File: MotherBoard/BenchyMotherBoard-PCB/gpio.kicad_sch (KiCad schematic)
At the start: 29 parts, among them J8 FAN-CONN, Q1 SQ2310ES_SOT23, Q2 MMBT2222A, SW1 BOOT-SEL, U27 TMP100NA, U28 TMP100NA, U4 AM6254ATCGGAALW, Y1 24MHz

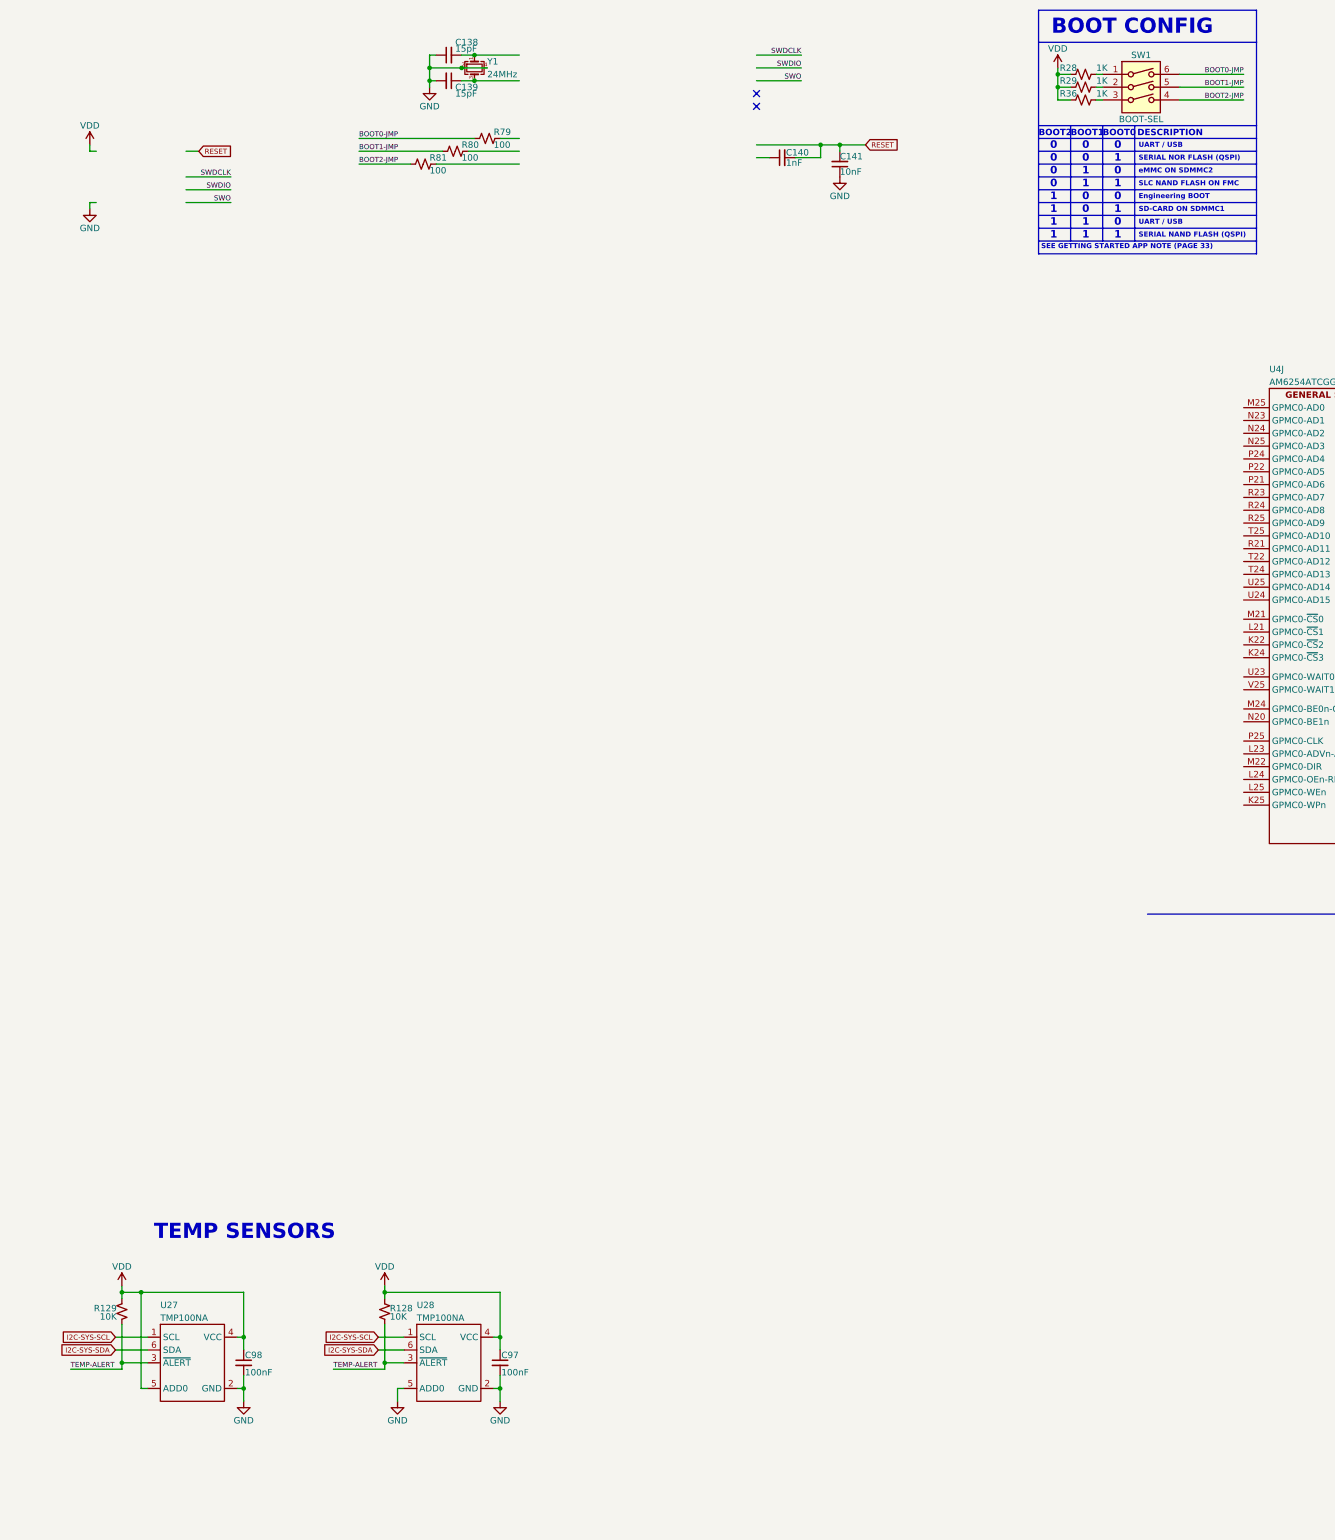
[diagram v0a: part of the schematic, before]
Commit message: Add new ethernet chip - KSZ9031
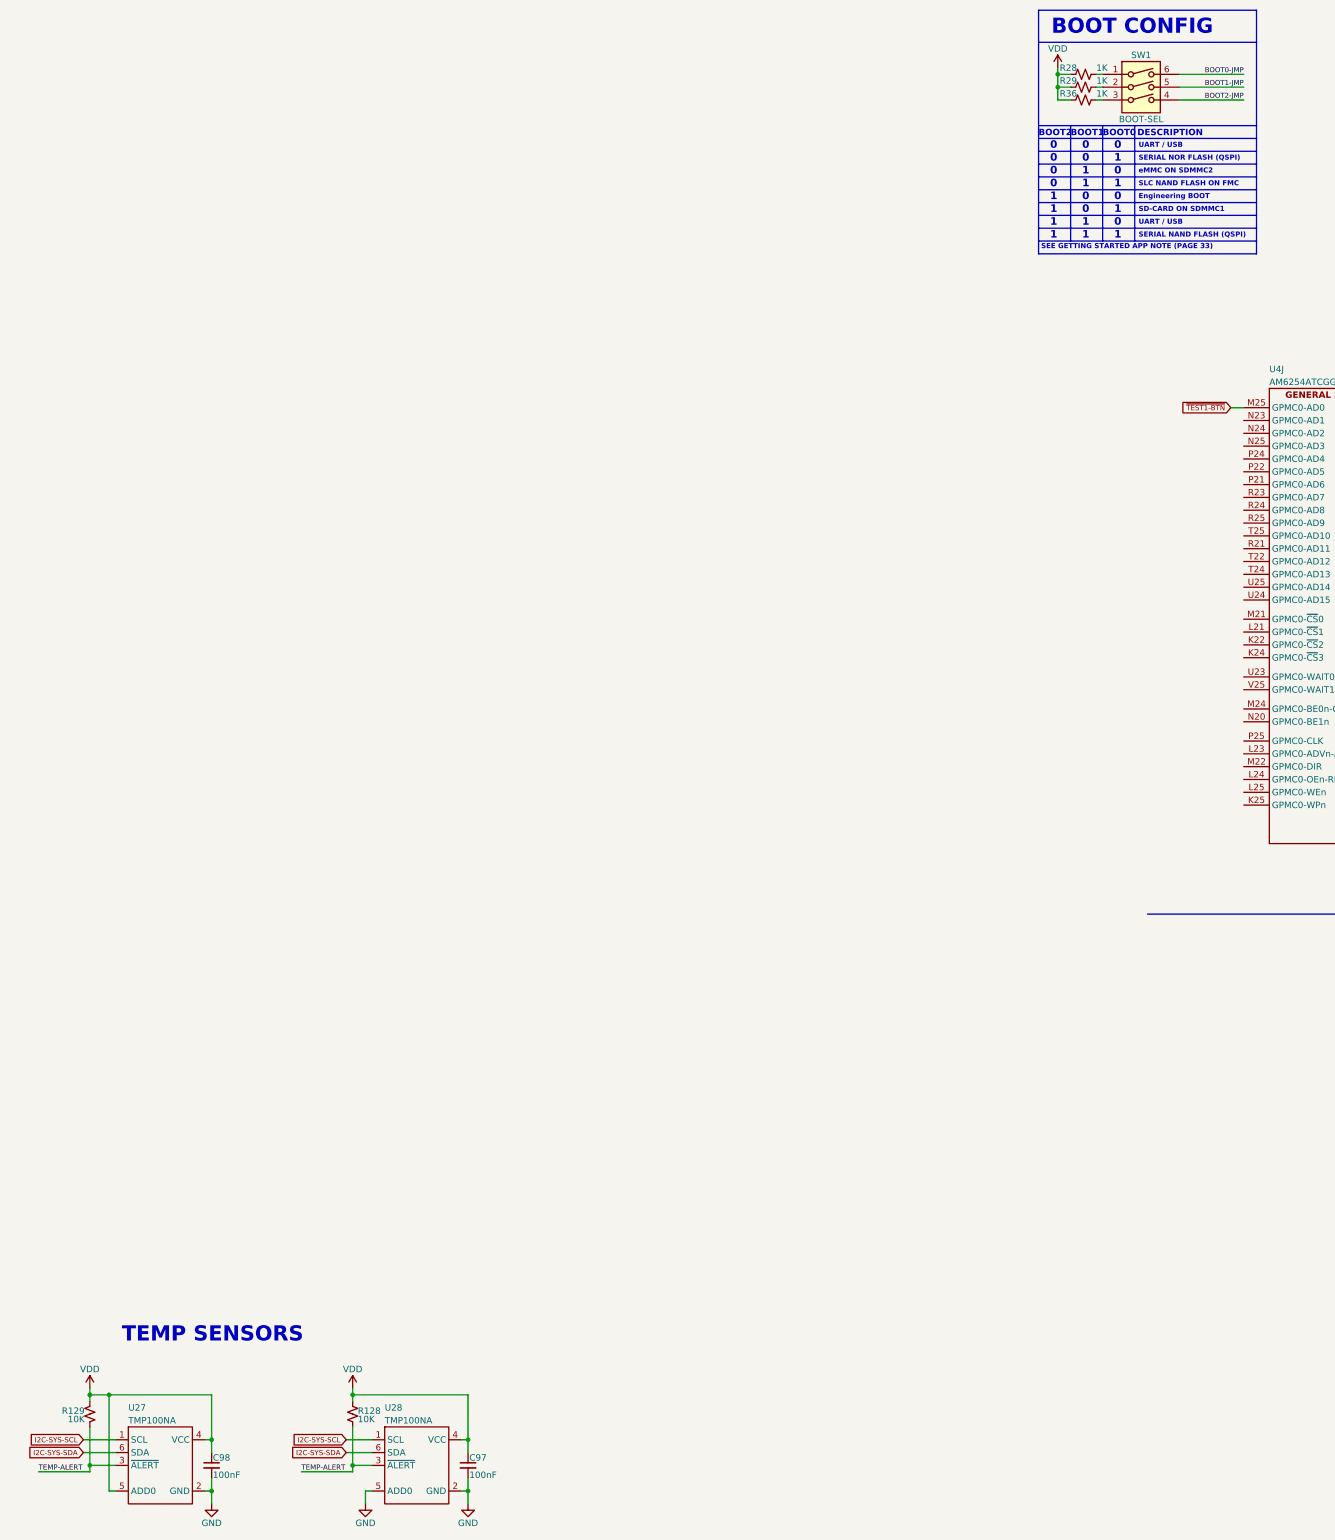
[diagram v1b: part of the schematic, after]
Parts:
- removed C138, C139: 15pF, Capacitor_SMD:C_0402_1005Metric, symbol Daxxn_Device:C
- removed C140: 1nF, Capacitor_SMD:C_0402_1005Metric, symbol Daxxn_Device:C
- removed C141: 10nF, Capacitor_SMD:C_0402_1005Metric, symbol Daxxn_Device:C
- removed R79, R80, R81: 100, Resistor_SMD:R_0402_1005Metric, symbol Daxxn_Device:R
- removed Y1: 24MHz, Daxxn_Passives:Crystal_SMD_4Pin_3.2x2.5mm, symbol Device:Crystal_GND24_Small
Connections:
- net ~{TEST1-BTN}: now reaches U4.M25 (GPMC0-AD0)
- no-connect marks 2 -> 0
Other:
- moved on the sheet: C97, C98, R128, R129, U27, U28

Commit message: (WIP) Almost done with schematic
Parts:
- removed Q2: MMBT2222A, Package_TO_SOT_SMD:SOT-23, symbol Daxxn_Transistors:MMBT2222A
- removed R28, R29, R36: 1K, Resistor_SMD:R_0402_1005Metric, symbol Daxxn_Device:R
- removed R89: 100, Resistor_SMD:R_0402_1005Metric, symbol Daxxn_Device:R
- removed SW1: BOOT-SEL, Button_Switch_SMD:SW_DIP_SPSTx03_Slide_Copal_CVS-03xB_W5.9mm_P1mm, symbol Switch:SW_DIP_x03
- added C418, C419: 100nF, Capacitor_SMD:C_0201_0603Metric, symbol Daxxn_Device:C
- Q1: value SQ2310ES_SOT23 -> SQ2310ES
- R90: value 1K -> 100
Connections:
- net VCC is gone; now on an unnamed net: R88.2
- net GND: now also C418.2, C419.2
- net VDD: now also R88.1, C418.1, C419.1
- net ~{TEST1-BTN}: no longer U4.M25 (GPMC0-AD0)
- net at R90.1: now also Q1.1 (G)
- net TEMP-ALERT renamed ~{TEMP-ALERT}
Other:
- note removed: "0"
- note removed: "1"
- note removed: "BOOT CONFIG"
- note removed: "BOOT0"
- note removed: "BOOT1"
- note removed: "BOOT2"
- note removed: "DESCRIPTION"
- note removed: "Engineering BOOT"
- note removed: "SD-CARD ON SDMMC1"
- note removed: "SEE GETTING STARTED APP NOTE (PAGE 33)"
- note removed: "SERIAL NAND FLASH (QSPI)"
- note removed: "SERIAL NOR FLASH (QSPI)"
- note removed: "SLC NAND FLASH ON FMC"
- note removed: "UART / USB"
- note removed: "eMMC ON SDMMC2"
- moved on the sheet: C97, J8, Q1, R128, R90, U28

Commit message: Start PCB layout
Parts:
- removed R128, R129: 10K, Resistor_SMD:R_0201_0603Metric, symbol Daxxn_Device:R
- removed U27, U28: TMP100NA, Daxxn_Packages:SOT-23-6, symbol Daxxn_Sensors:TMP100NA
- added C316, C317: 100nF, Capacitor_SMD:C_0201_0603Metric, symbol Daxxn_Device:C
- added R120 (x16): 1K, Resistor_SMD:R_0201_0603Metric, symbol Daxxn_Device:R
- added R120 (x16): 100K, Resistor_SMD:R_0402_1005Metric, symbol Daxxn_Device:R
- added R120 (x4): 1K, Resistor_SMD:R_0402_1005Metric, symbol Daxxn_Device:R
- added R120 (x2): 10K, Resistor_SMD:R_0402_1005Metric, symbol Daxxn_Device:R
- added SW1, SW3, SW4, SW5: 221AMC16R, Daxxn_Switches:221AMC16R, symbol Switch:SW_Coded_SH-7070
- added U24: PI4IOE5V6408, Daxxn_Packages:UQFN-16-ZTA_DIO-M, symbol Daxxn_IC:PI4IOE5V6408
- added U25, U26: TMP100NA, Daxxn_Packages:SOT-23-6, symbol Daxxn_Sensors:TMP100NA
- renumbered C98 to C318, C418 to C319, C97 to C320, C419 to C321, J8 to J5, Q1 to Q5, R88 to R126, R90 to R127, R131 to R85, R130 to R86, R132 to R87, R133 to R88
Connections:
- net GND: now also C316.2, C317.2, R120.2, R120.2, R120.2, R120.2, R120.2, R120.2, R120.2, R120.2, R120.2, R120.2, R120.2, R120.2, R120.2, R120.2, R120.2, R120.2, U24.16 (GND), U24.9 (ADDR), U25.2 (GND), U25.3 (ADD1), U25.5 (ADD0), U26.2 (GND), U26.3 (ADD1)
- net I2C-MAIN-SCL: now also U24.13 (SCL)
- net I2C-MAIN-SDA: now also U24.14 (SDA)
- net I2C-SYS-SCL: now also U25.1 (SCL), U26.1 (SCL)
- net I2C-SYS-SDA: now also U25.6 (SDA), U26.6 (SDA)
- net RELAY-BUS1: now also U24.12 (P0)
- net RELAY-BUS2: now also U24.11 (P1)
- net RELAY-BUS3: now also U24.8 (P2)
- net RELAY-BUS4: now also U24.7 (P3)
- net RELAY-BUS5: now also U24.6 (P4)
- net RELAY-BUS6: now also U24.5 (P5)
- net SD-CARD-PWR-SEL: now also U4.N25 (GPMC0-AD3), R120.2
- net VDD: now also C316.1, C317.1, R120.1, R120.1, U24.15 (VDDB), U24.2 (VDDP), U25.4 (VCC), U26.4 (VCC)
- net ~{HDMI-INT}: now also U4.P24 (GPMC0-AD4), R120.2
- net ~{HDMI-RESET}: now also U4.V25 (GPMC0-WAIT1)
- net ~{RESET-EMMC}: now also U4.K24 (GPMC0-~{CS}3)
- net ~{RESET-OSPI}: now also U4.M21 (GPMC0-~{CS}0)
- net ~{RESET-USB}: now also U4.U23 (GPMC0-WAIT0)
- net ~{SDCARD1-EN}: now also U4.K22 (GPMC0-~{CS}2)
- net ~{SDCARD2-EN}: now also U4.L21 (GPMC0-~{CS}1)
- net ~{TEST1-BTN}: now also U4.N24 (GPMC0-AD2), R120.2
- net ~{RESET-USB-HUB}: now reaches U4.M24 (GPMC0-BE0n-CLE)
- net FAN-EN: now reaches U4.M25 (GPMC0-AD0)
- net FAN-EN: now also R120.2
- net ~{TEST2-BTN}: now reaches U4.N23 (GPMC0-AD1)
- net ~{TEST2-BTN}: now also R120.2
- net OVERTEMP-IND: now reaches U4.P21 (GPMC0-AD6)
- net TEST-IND: now reaches U4.P22 (GPMC0-AD5)
- net TEST-IND: now also R120.2
- net VOUT0-DATA19: now reaches U4.R21 (GPMC0-AD11)
- net VOUT0-DATA19: now also R120.2
- net VOUT0-DATA16: now reaches U4.R24 (GPMC0-AD8)
- net VOUT0-DATA16: now also R120.2
- net VOUT0-DATA17: now reaches U4.R25 (GPMC0-AD9)
- net VOUT0-DATA17: now also R120.2
- net VOUT0-DATA20: now reaches U4.T22 (GPMC0-AD12)
- net VOUT0-DATA20: now also R120.2
- net VOUT0-DATA21: now reaches U4.T24 (GPMC0-AD13)
- net VOUT0-DATA21: now also R120.2
- net VOUT0-DATA18: now reaches U4.T25 (GPMC0-AD10)
- net VOUT0-DATA18: now also R120.2
- net VOUT0-DATA23: now reaches U4.U24 (GPMC0-AD15)
- net VOUT0-DATA23: now also R120.2
- net VOUT0-DATA22: now reaches U4.U25 (GPMC0-AD14)
- net VOUT0-DATA22: now also R120.2
- new net: R120.2, SW3.C
- new net: R120.2, U24.1 (~{INT})
- new net: R120.2, SW4.C
- new net: R120.2, SW5.C
- new net: R120.2, SW1.C
- new net BOOTMODE00: R120.1, R120.1, SW1.1
- new net BOOTMODE01: R120.1, R120.1, SW1.2
- new net BOOTMODE02: R120.1, R120.1, SW1.4
- new net BOOTMODE03: R120.1, R120.1, SW1.8
- new net BOOTMODE04: R120.1, R120.1, SW3.1
- new net BOOTMODE05: R120.1, R120.1, SW3.2
- new net BOOTMODE06: R120.1, R120.1, SW3.4
- new net BOOTMODE07: R120.1, R120.1, SW3.8
- new net BOOTMODE08: R120.1, R120.1, SW4.1
- new net BOOTMODE09: R120.1, R120.1, SW4.2
- new net BOOTMODE10: R120.1, R120.1, SW4.4
- new net BOOTMODE11: R120.1, R120.1, SW4.8
- new net BOOTMODE12: R120.1, R120.1, SW5.1
- new net BOOTMODE13: R120.1, R120.1, SW5.2
- new net BOOTMODE14: R120.1, R120.1, SW5.4
- new net BOOTMODE15: R120.1, R120.1, SW5.8
- new net DVDD: R120.1, R120.1, R120.1, R120.1
- new net ~{RESET-STATUS}: R120.2, U24.10 (~{RESET})
- no-connect marks 0 -> 3
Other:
- note added: "ADDRESS : 0x43"
- note added: "MEMORY TEMP ADDRESS : 0x49"
- note added: "SOC TEMP ADDRESS : 0x48"

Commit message: (WIP) Still laying out PCB
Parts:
- removed C316, C317: 100nF, Capacitor_SMD:C_0201_0603Metric, symbol Daxxn_Device:C
- removed R120 (x2): 10K, Resistor_SMD:R_0402_1005Metric, symbol Daxxn_Device:R
- removed U24: PI4IOE5V6408, Daxxn_Packages:UQFN-16-ZTA_DIO-M, symbol Daxxn_IC:PI4IOE5V6408
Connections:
- net RELAY-BUS1: now also U4.P25 (GPMC0-CLK)
- net RELAY-BUS2: now also U4.L23 (GPMC0-ADVn-ALE)
- net RELAY-BUS3: now also U4.M22 (GPMC0-DIR)
- net RELAY-BUS4: now also U4.L24 (GPMC0-OEn-REn)
- net RELAY-BUS5: now also U4.L25 (GPMC0-WEn)
- net RELAY-BUS6: now also U4.K25 (GPMC0-WPn)
- no-connect marks 3 -> 11
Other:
- note removed: "ADDRESS : 0x43"

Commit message: Replacing motherboard and more - SAVE
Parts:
- renumbered R120 to R100, R120 to R101, R120 to R102, R120 to R103, R120 to R104, R120 to R105, R120 to R106, R120 to R107, R120 to R108, R120 to R109, R120 to R110, R120 to R111, R120 to R112, R120 to R113, R120 to R114, R120 to R115, R120 to R116, R120 to R117, R120 to R118, R120 to R121, R120 to R122, R120 to R123, R120 to R124, R120 to R125, R120 to R84, R120 to R89, R120 to R90, R120 to R91, R120 to R92, R120 to R93, R120 to R94, R120 to R95, R120 to R96, R120 to R97, R120 to R98, R120 to R99, SW3 to SW2, SW4 to SW3, SW5 to SW4, U4 to U1
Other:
- note added: "NEED TO MATCH THIS WITH THE INTERFACES ALREADY BUILT FOR THE EXISTING BENCHY BOARDS."
- note added: "REPLACE THIS WITH A JUMPER HEADER."
